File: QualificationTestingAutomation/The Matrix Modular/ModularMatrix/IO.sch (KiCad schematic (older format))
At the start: 10 parts, among them J1 Conn_02x32_Counter_Clockwise_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, J5 Conn_02x32_Counter_Clockwise_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, J6 Banana Jack, J7 Banana Jack, J8 Banana Jack, J9 Banana Jack

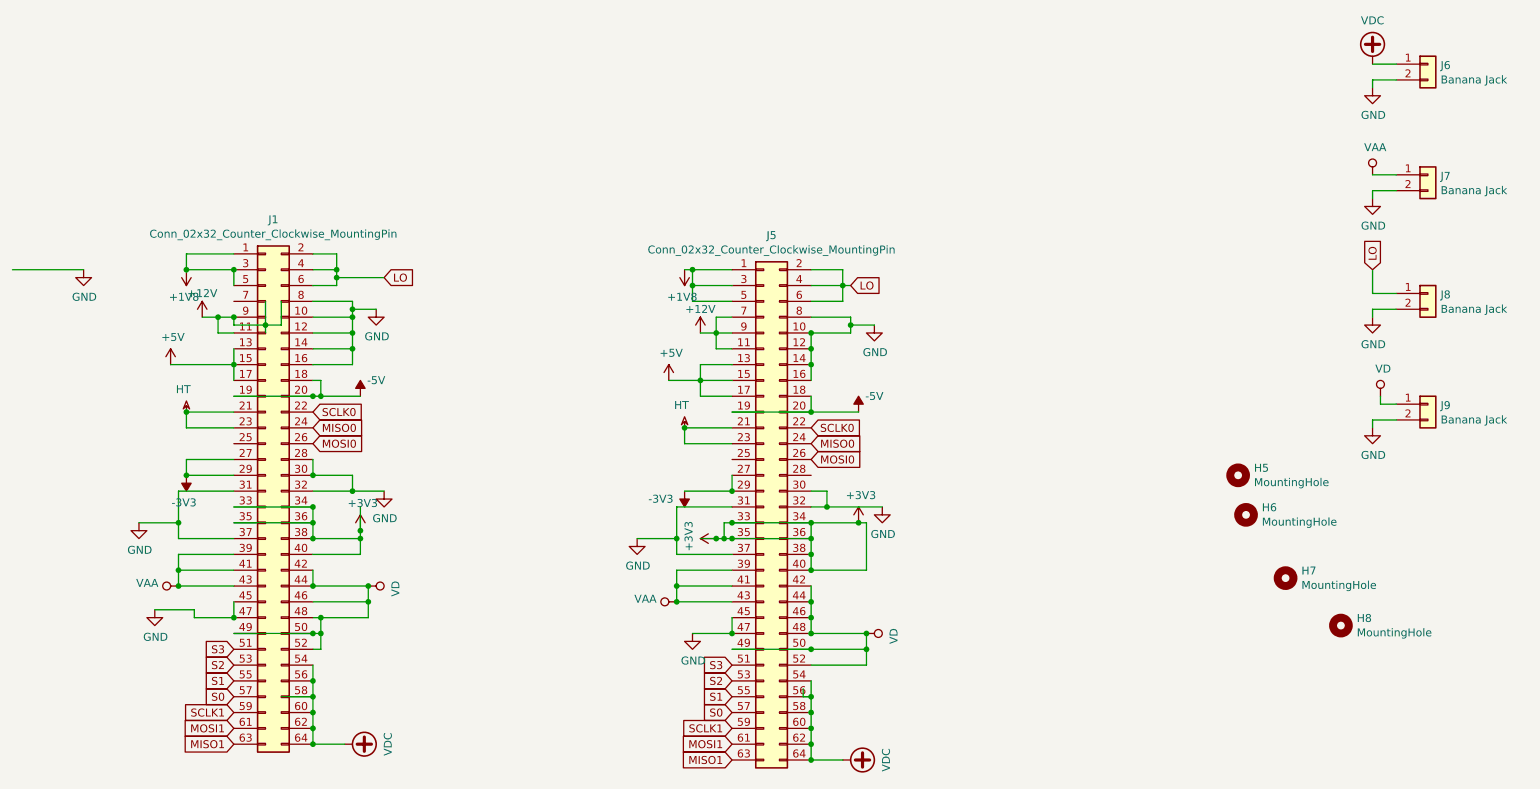
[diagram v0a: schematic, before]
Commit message: IO clean up added the 1v25 reference to Matrix Changed Some of the labels to more legible names.
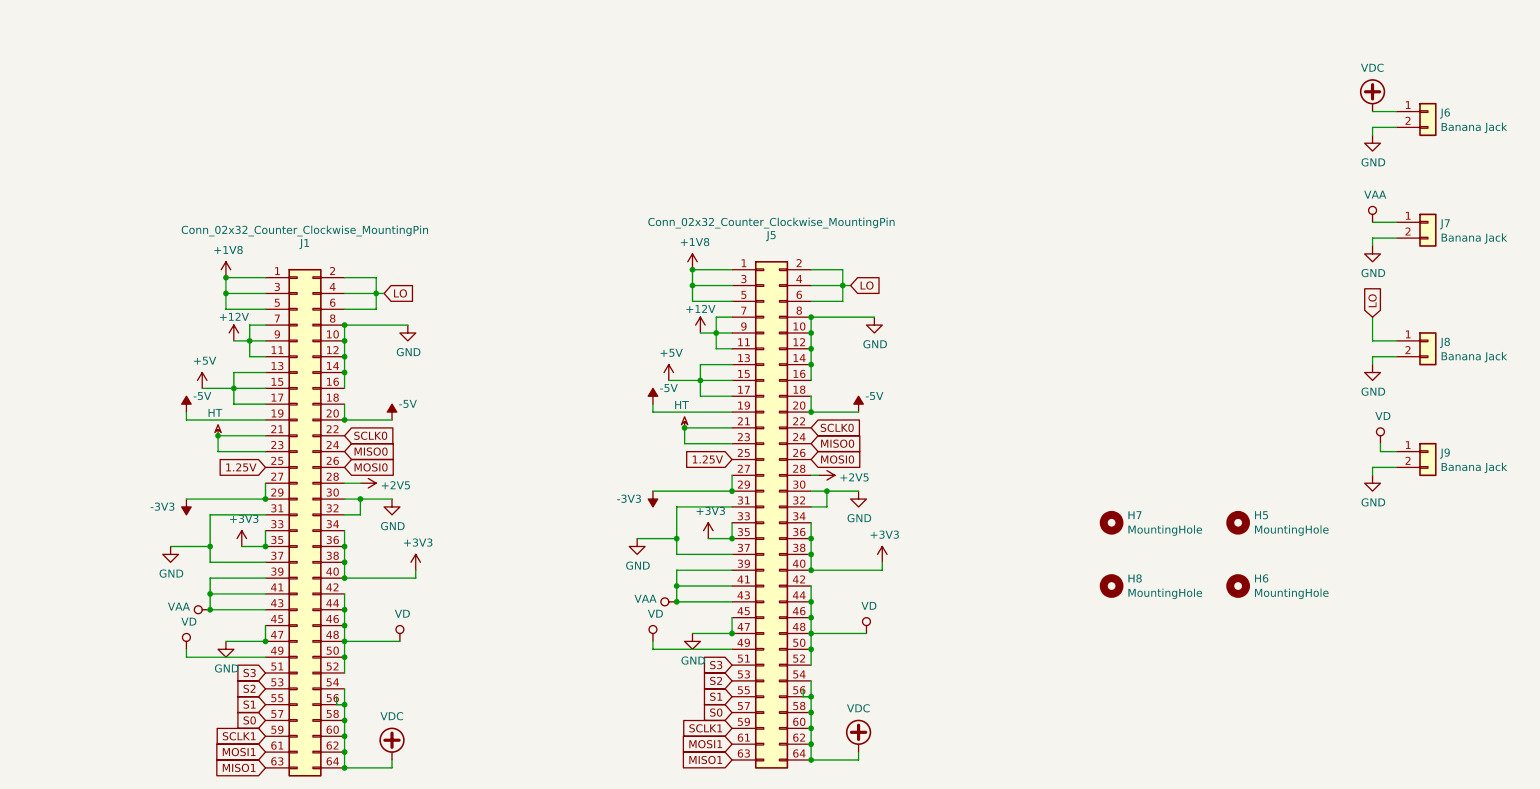
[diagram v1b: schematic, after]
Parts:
- J1, J5: footprint Connector:PinHeader_2x32_P2.00mm_Vertical_Clockwise -> Connector:PinHeader_2x32_P2.00mm_VerticalOpp
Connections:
- net labels added: +2V5, 1.25V
- wire segments 195 -> 170
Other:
- moved on the sheet: H5, H6, H7, H8, J6, J7, J8, J9
